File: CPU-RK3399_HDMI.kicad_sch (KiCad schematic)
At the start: 15 parts, among them U1 RK3399

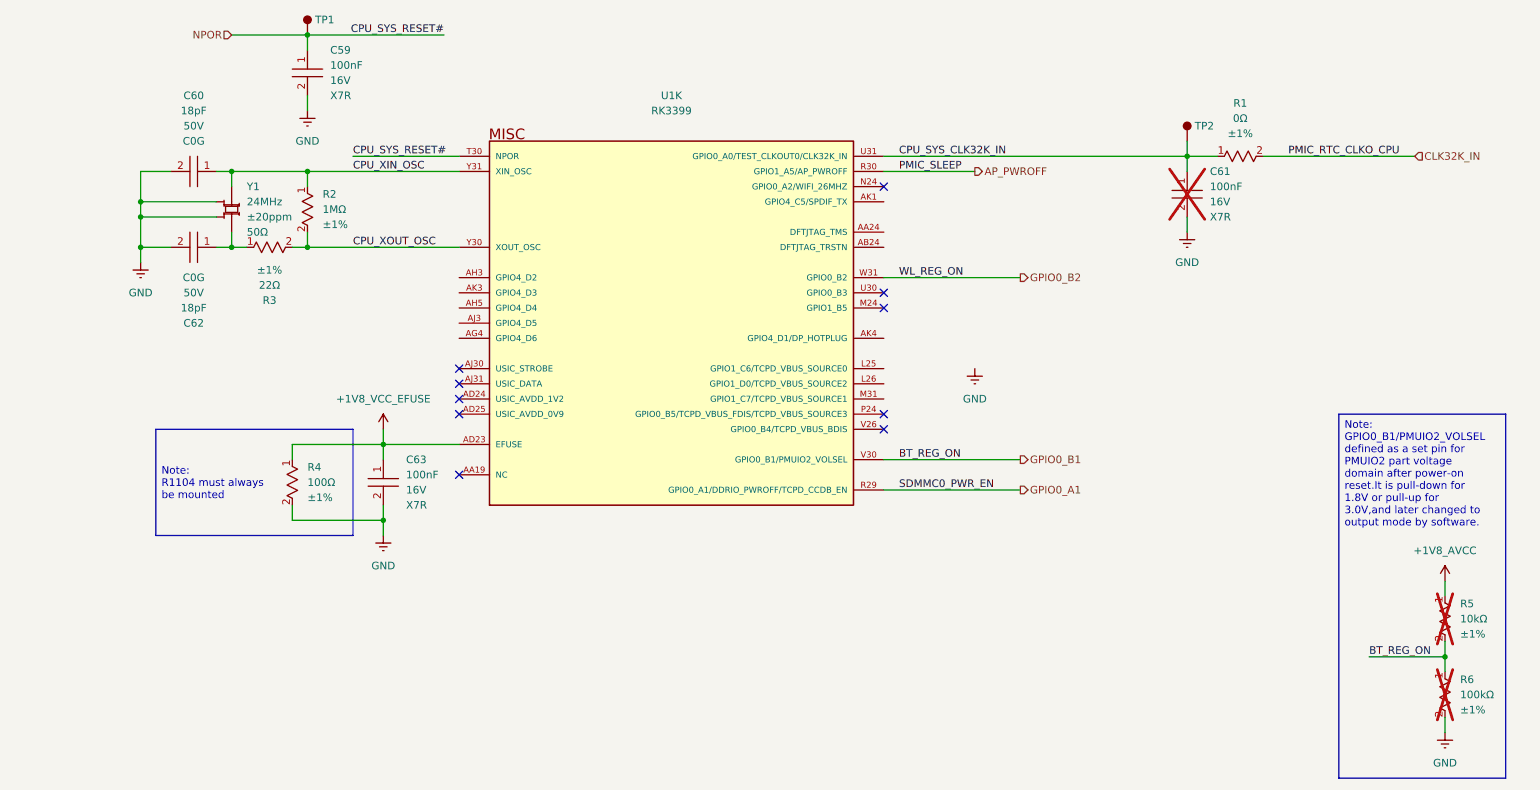
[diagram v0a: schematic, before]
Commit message: update schematic
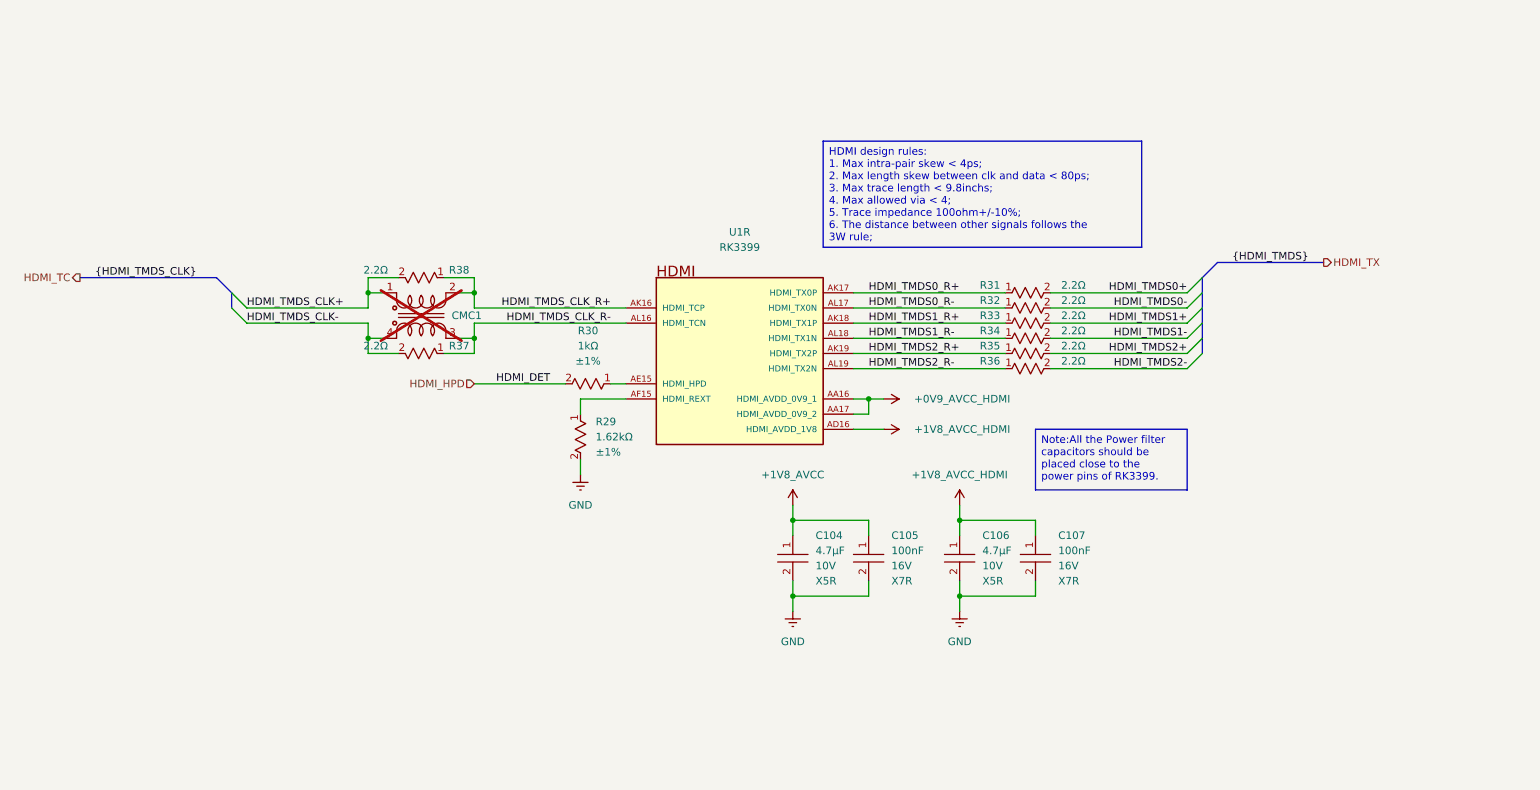
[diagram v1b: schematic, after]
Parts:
- removed C59, C61, C63: ~, footprints:CAPC1005X50N, symbol component_library:Capacitors/CL05B104KO5NNNC
- removed C60, C62: ~, footprints:CAPC1005X50N, symbol component_library:Capacitors/0402CG180J500NT
- removed R1: ~, footprints:RESC1005X35N, symbol component_library:Resistors/0402WGF0000TCE
- removed R2: ~, footprints:RESC1005X35N, symbol component_library:Resistors/0402WGF1004TCE
- removed R3: ~, footprints:RESC1005X35N, symbol component_library:Resistors/0402WGF220JTCE
- removed R4: ~, footprints:RESC1005X35N, symbol component_library:Resistors/0402WGF1000TCE
- removed R5: ~, footprints:RESC1005X35N, symbol component_library:Resistors/0402WGF1002TCE
- removed R6: ~, footprints:RESC1005X35N, symbol component_library:Resistors/0402WGF1003TCE
- removed TP1, TP2: ~, footprints:, symbol component_library:Mechanical/Test_Point
- removed U1: RK3399, footprints:BGA828C65P31X31_2100X2100X161, symbol component_library:System On Chip (SoC)/RK3399
- removed Y1: ~, footprints:, symbol component_library:Crystals, Oscillators, Resonators/X322524MOB4SI
- added C104, C106: ~, footprints:CAPC1005X50N, symbol component_library:Capacitors/CL05A475MP5NRNC
- added C105, C107: ~, footprints:CAPC1005X50N, symbol component_library:Capacitors/CL05B104KO5NNNC
- added CMC1: ~, footprints:, symbol component_library:Filters/DLW21SH900HQ2L
- added R29: ~, footprints:RESC1005X35N, symbol component_library:Resistors/0402WGF1621TCE
- added R30: ~, footprints:RESC1005X35N, symbol component_library:Resistors/0402WGF1001TCE
- added R31, R32, R33, R34, R35, R36, R37, R38: ~, footprints:RESC1005X35N, symbol component_library:Resistors/CQ02WGF220KTCE
- added U1: RK3399, footprints:BGA828C65P31X31_2100X2100X161, symbol component_library:System On Chip (SoC)/RK3399
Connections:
- net +1V8_AVCC: now also C104.1, C105.1
- net GND: now also C104.2, C105.2, C106.2, C107.2, R29.2
- new net: R29.1, U1.AF15 (HDMI_REXT)
- new net: R30.1, U1.AE15 (HDMI_HPD)
- new net +0V9_AVCC_HDMI: U1.AA16 (HDMI_AVDD_0V9_1), U1.AA17 (HDMI_AVDD_0V9_2)
- new net +1V8_AVCC_HDMI: C106.1, C107.1, U1.AD16 (HDMI_AVDD_1V8)
- new net HDMI_HPD: R30.2
- new net HDMI_TMDS0+: R31.2
- new net HDMI_TMDS0-: R32.2
- new net HDMI_TMDS0_R+: R31.1, U1.AK17 (HDMI_TX0P)
- new net HDMI_TMDS0_R-: R32.1, U1.AL17 (HDMI_TX0N)
- new net HDMI_TMDS1+: R33.2
- new net HDMI_TMDS1-: R34.2
- new net HDMI_TMDS1_R+: R33.1, U1.AK18 (HDMI_TX1P)
- new net HDMI_TMDS1_R-: R34.1, U1.AL18 (HDMI_TX1N)
- new net HDMI_TMDS2+: R35.2
- new net HDMI_TMDS2-: R36.2
- new net HDMI_TMDS2_R+: R35.1, U1.AK19 (HDMI_TX2P)
- new net HDMI_TMDS2_R-: R36.1, U1.AL19 (HDMI_TX2N)
- new net HDMI_TMDS_CLK+: CMC1.1, R38.2
- new net HDMI_TMDS_CLK-: CMC1.4, R37.2
- new net HDMI_TMDS_CLK_R+: CMC1.2, R38.1, U1.AK16 (HDMI_TCP)
- new net HDMI_TMDS_CLK_R-: CMC1.3, R37.1, U1.AL16 (HDMI_TCN)
- no-connect marks 10 -> 0
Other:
- title: CPU-RK3399 PMU -> CPU-RK3399 HDMI Controller

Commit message: update design power
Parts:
- renumbered C104 to C159, C105 to C160, C106 to C161, C107 to C162, R38 to R52, R31 to R53, R32 to R54, R33 to R55, R34 to R56, R37 to R57, R35 to R58, R36 to R59, R30 to R60, R29 to R61, U1 to U2
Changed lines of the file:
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@@
 		(on_board yes)
 		(dnp no)
-		(property "Reference" "C104"
+		(property "Reference" "C159"
 			(at 163.83 119.3799 0)
 			(effects
@@
 			(project ""
 				(path "/ebc9dc57-8b05-484a-a5cd-c53b1efc71d3/a7299b18-4123-434b-8c69-0b9524fffa12/25d97e15-4196-4e44-984c-f8c0409a1a6b"
-					(reference "C104")
+					(reference "C159")
 					(unit 1)
 				)
@@
 		(on_board yes)
 		(dnp no)
-		(property "Reference" "#PWR0112"
+		(property "Reference" "#PWR0199"
 			(at 187.96 118.11 0)
 			(effects
@@
 			(project "VESA-SBC3399"
 				(path "/ebc9dc57-8b05-484a-a5cd-c53b1efc71d3/a7299b18-4123-434b-8c69-0b9524fffa12/25d97e15-4196-4e44-984c-f8c0409a1a6b"
-					(reference "#PWR0112")
+					(reference "#PWR0199")
 					(unit 1)
 				)
@@
 		(on_board yes)
 		(dnp no)
-		(property "Reference" "C105"
+		(property "Reference" "C160"
 			(at 176.53 119.3799 0)
 			(effects
@@
 			(project ""
 				(path "/ebc9dc57-8b05-484a-a5cd-c53b1efc71d3/a7299b18-4123-434b-8c69-0b9524fffa12/25d97e15-4196-4e44-984c-f8c0409a1a6b"
-					(reference "C105")
+					(reference "C160")
 					(unit 1)
 				)
@@
 		(on_board yes)
 		(dnp no)
-		(property "Reference" "R36"
+		(property "Reference" "R59"
 			(at 193.04 90.17 0)
 			(effects
@@
 			(project "VESA-SBC3399"
 				(path "/ebc9dc57-8b05-484a-a5cd-c53b1efc71d3/a7299b18-4123-434b-8c69-0b9524fffa12/25d97e15-4196-4e44-984c-f8c0409a1a6b"
-					(reference "R36")
+					(reference "R59")
 					(unit 1)
 				)
@@
 		(on_board yes)
 		(dnp no)
-		(property "Reference" "R38"
+		(property "Reference" "R52"
 			(at 104.14 74.93 0)
 			(effects
@@
 			(project "VESA-SBC3399"
 				(path "/ebc9dc57-8b05-484a-a5cd-c53b1efc71d3/a7299b18-4123-434b-8c69-0b9524fffa12/25d97e15-4196-4e44-984c-f8c0409a1a6b"
-					(reference "R38")
+					(reference "R52")
 					(unit 1)
 				)
@@
 		(dnp no)
 		(fields_autoplaced yes)
-		(property "Reference" "R29"
+		(property "Reference" "R61"
 			(at 127 100.3299 90)
 			(effects
@@
 			(project "VESA-SBC3399"
 				(path "/ebc9dc57-8b05-484a-a5cd-c53b1efc71d3/a7299b18-4123-434b-8c69-0b9524fffa12/25d97e15-4196-4e44-984c-f8c0409a1a6b"
-					(reference "R29")
+					(reference "R61")
 					(unit 1)
 				)
@@
 		(dnp no)
 		(fields_autoplaced yes)
-		(property "Reference" "#PWR0108"
+		(property "Reference" "#PWR0197"
 			(at 124.46 115.57 0)
 			(effects
@@
 			(project "VESA-SBC3399"
 				(path "/ebc9dc57-8b05-484a-a5cd-c53b1efc71d3/a7299b18-4123-434b-8c69-0b9524fffa12/25d97e15-4196-4e44-984c-f8c0409a1a6b"
-					(reference "#PWR0108")
+					(reference "#PWR0197")
 					(unit 1)
 				)
@@
 		(on_board yes)
 		(dnp no)
-		(property "Reference" "#PWR0111"
+		(property "Reference" "#PWR0198"
 			(at 160.02 118.11 0)
 			(effects
@@
 			(project "VESA-SBC3399"
 				(path "/ebc9dc57-8b05-484a-a5cd-c53b1efc71d3/a7299b18-4123-434b-8c69-0b9524fffa12/25d97e15-4196-4e44-984c-f8c0409a1a6b"
-					(reference "#PWR0111")
+					(reference "#PWR0198")
 					(unit 1)
 				)
@@
 		(on_board yes)
 		(dnp no)
-		(property "Reference" "R32"
+		(property "Reference" "R54"
 			(at 193.04 80.01 0)
 			(effects
@@
 			(project "VESA-SBC3399"
 				(path "/ebc9dc57-8b05-484a-a5cd-c53b1efc71d3/a7299b18-4123-434b-8c69-0b9524fffa12/25d97e15-4196-4e44-984c-f8c0409a1a6b"
-					(reference "R32")
+					(reference "R54")
 					(unit 1)
 				)
@@
 		(on_board yes)
 		(dnp no)
-		(property "Reference" "C106"
+		(property "Reference" "C161"
 			(at 191.77 119.3799 0)
 			(effects
@@
 			(project "VESA-SBC3399"
 				(path "/ebc9dc57-8b05-484a-a5cd-c53b1efc71d3/a7299b18-4123-434b-8c69-0b9524fffa12/25d97e15-4196-4e44-984c-f8c0409a1a6b"
-					(reference "C106")
+					(reference "C161")
 					(unit 1)
 				)
@@
 		(dnp no)
 		(fields_autoplaced yes)
-		(property "Reference" "#PWR0114"
+		(property "Reference" "#PWR0201"
 			(at 187.96 138.43 0)
 			(effects
@@
 			(project "VESA-SBC3399"
 				(path "/ebc9dc57-8b05-484a-a5cd-c53b1efc71d3/a7299b18-4123-434b-8c69-0b9524fffa12/25d97e15-4196-4e44-984c-f8c0409a1a6b"
-					(reference "#PWR0114")
+					(reference "#PWR0201")
 					(unit 1)
 				)
@@
 		(on_board yes)
 		(dnp no)
-		(property "Reference" "R34"
+		(property "Reference" "R56"
 			(at 193.04 85.09 0)
 			(effects
@@
 			(project "VESA-SBC3399"
 				(path "/ebc9dc57-8b05-484a-a5cd-c53b1efc71d3/a7299b18-4123-434b-8c69-0b9524fffa12/25d97e15-4196-4e44-984c-f8c0409a1a6b"
-					(reference "R34")
+					(reference "R56")
 					(unit 1)
 				)
@@
 		(on_board yes)
 		(dnp no)
-		(property "Reference" "C107"
+		(property "Reference" "C162"
 			(at 204.47 119.3799 0)
 			(effects
@@
 			(project "VESA-SBC3399"
 				(path "/ebc9dc57-8b05-484a-a5cd-c53b1efc71d3/a7299b18-4123-434b-8c69-0b9524fffa12/25d97e15-4196-4e44-984c-f8c0409a1a6b"
-					(reference "C107")
+					(reference "C162")
 					(unit 1)
 				)
@@
 		(on_board yes)
 		(dnp no)
-		(property "Reference" "#PWR0109"
+		(property "Reference" "#PWR0195"
 			(at 171.45 96.52 0)
 			(effects
@@
 			(project "VESA-SBC3399"
 				(path "/ebc9dc57-8b05-484a-a5cd-c53b1efc71d3/a7299b18-4123-434b-8c69-0b9524fffa12/25d97e15-4196-4e44-984c-f8c0409a1a6b"
-					(reference "#PWR0109")
+					(reference "#PWR0195")
 					(unit 1)
 				)
@@
 		(dnp no)
 		(fields_autoplaced yes)
-		(property "Reference" "U1"
+		(property "Reference" "U2"
 			(at 151.13 68.58 0)
 			(effects
@@
 			(project ""
 				(path "/ebc9dc57-8b05-484a-a5cd-c53b1efc71d3/a7299b18-4123-434b-8c69-0b9524fffa12/25d97e15-4196-4e44-984c-f8c0409a1a6b"
-					(reference "U1")
+					(reference "U2")
 					(unit 18)
 				)
@@
 		(dnp no)
 		(fields_autoplaced yes)
-		(property "Reference" "#PWR0113"
+		(property "Reference" "#PWR0200"
 			(at 160.02 138.43 0)
 			(effects
@@
 			(project "VESA-SBC3399"
 				(path "/ebc9dc57-8b05-484a-a5cd-c53b1efc71d3/a7299b18-4123-434b-8c69-0b9524fffa12/25d97e15-4196-4e44-984c-f8c0409a1a6b"
-					(reference "#PWR0113")
+					(reference "#PWR0200")
 					(unit 1)
 				)
@@
 		(dnp no)
 		(fields_autoplaced yes)
-		(property "Reference" "R30"
+		(property "Reference" "R60"
 			(at 125.73 85.09 0)
 			(effects
@@
 			(project ""
 				(path "/ebc9dc57-8b05-484a-a5cd-c53b1efc71d3/a7299b18-4123-434b-8c69-0b9524fffa12/25d97e15-4196-4e44-984c-f8c0409a1a6b"
-					(reference "R30")
+					(reference "R60")
 					(unit 1)
 				)
@@
 		(on_board yes)
 		(dnp no)
-		(property "Reference" "R37"
+		(property "Reference" "R57"
 			(at 104.14 87.63 0)
 			(effects
@@
 			(project "VESA-SBC3399"
 				(path "/ebc9dc57-8b05-484a-a5cd-c53b1efc71d3/a7299b18-4123-434b-8c69-0b9524fffa12/25d97e15-4196-4e44-984c-f8c0409a1a6b"
-					(reference "R37")
+					(reference "R57")
 					(unit 1)
 				)
@@
 		(on_board yes)
 		(dnp no)
-		(property "Reference" "R33"
+		(property "Reference" "R55"
 			(at 193.04 82.55 0)
 			(effects
@@
 			(project "VESA-SBC3399"
 				(path "/ebc9dc57-8b05-484a-a5cd-c53b1efc71d3/a7299b18-4123-434b-8c69-0b9524fffa12/25d97e15-4196-4e44-984c-f8c0409a1a6b"
-					(reference "R33")
+					(reference "R55")
 					(unit 1)
 				)
@@
 		(on_board yes)
 		(dnp no)
-		(property "Reference" "#PWR0110"
+		(property "Reference" "#PWR0196"
 			(at 171.45 101.6 0)
 			(effects
@@
 			(project "VESA-SBC3399"
 				(path "/ebc9dc57-8b05-484a-a5cd-c53b1efc71d3/a7299b18-4123-434b-8c69-0b9524fffa12/25d97e15-4196-4e44-984c-f8c0409a1a6b"
-					(reference "#PWR0110")
+					(reference "#PWR0196")
 					(unit 1)
 				)
@@
 		(on_board yes)
 		(dnp no)
-		(property "Reference" "R31"
+		(property "Reference" "R53"
 			(at 193.04 77.47 0)
 			(effects
@@
 			(project ""
 				(path "/ebc9dc57-8b05-484a-a5cd-c53b1efc71d3/a7299b18-4123-434b-8c69-0b9524fffa12/25d97e15-4196-4e44-984c-f8c0409a1a6b"
-					(reference "R31")
+					(reference "R53")
 					(unit 1)
 				)
@@
 		(on_board yes)
 		(dnp no)
-		(property "Reference" "R35"
+		(property "Reference" "R58"
 			(at 193.04 87.63 0)
 			(effects
@@
 			(project "VESA-SBC3399"
 				(path "/ebc9dc57-8b05-484a-a5cd-c53b1efc71d3/a7299b18-4123-434b-8c69-0b9524fffa12/25d97e15-4196-4e44-984c-f8c0409a1a6b"
-					(reference "R35")
+					(reference "R58")
 					(unit 1)
 				)
